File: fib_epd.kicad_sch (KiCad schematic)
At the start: 58 parts, among them J4 ED060SC4, J5 ED060SC7, J6 ED097OC4, J7 30PIN_05PITCH, U1 TPS651851RSLT, U4 ESP32-S3-WROOM-1U

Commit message: added port expander and level shifters, routed peripherals fixed most drc errors, assigned gpios etc.
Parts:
- R7: footprint Resistor_SMD:R_0402_1005Metric -> Resistor_SMD:R_0603_1608Metric
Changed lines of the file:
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@@
 			)
 		)
-		(property "Footprint" "Resistor_SMD:R_0402_1005Metric"
+		(property "Footprint" "Resistor_SMD:R_0603_1608Metric"
 			(at 29.21 33.02 0)
 			(effects

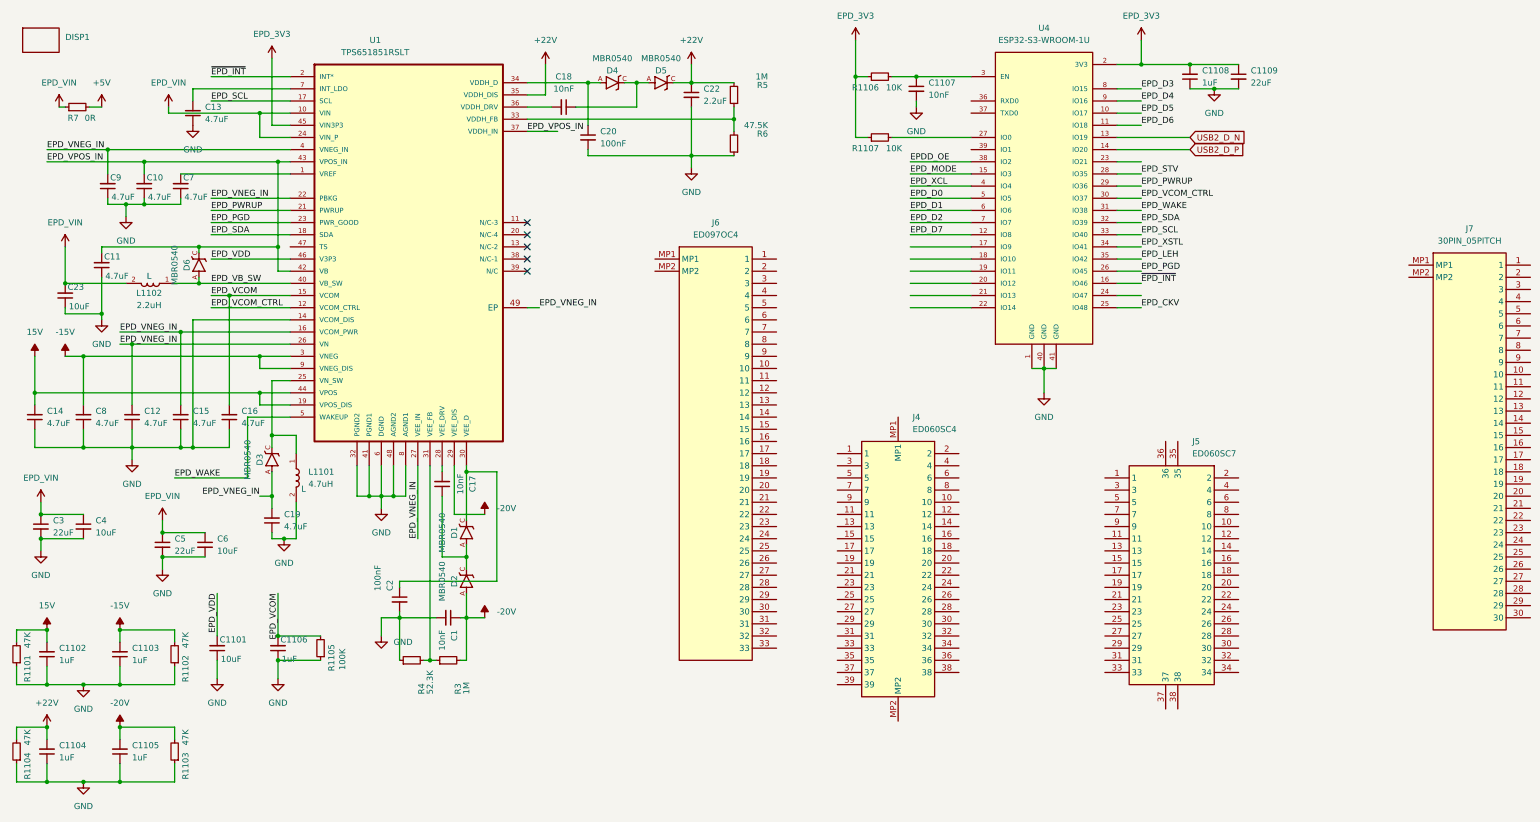
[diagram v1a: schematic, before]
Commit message: routed epd displays, added testpoints and all the little checks and fixe, (regrettably) removed the i80 connector, 99% there, need to double check some things add peripheral connectors, shared-ish storage and vias vias vias
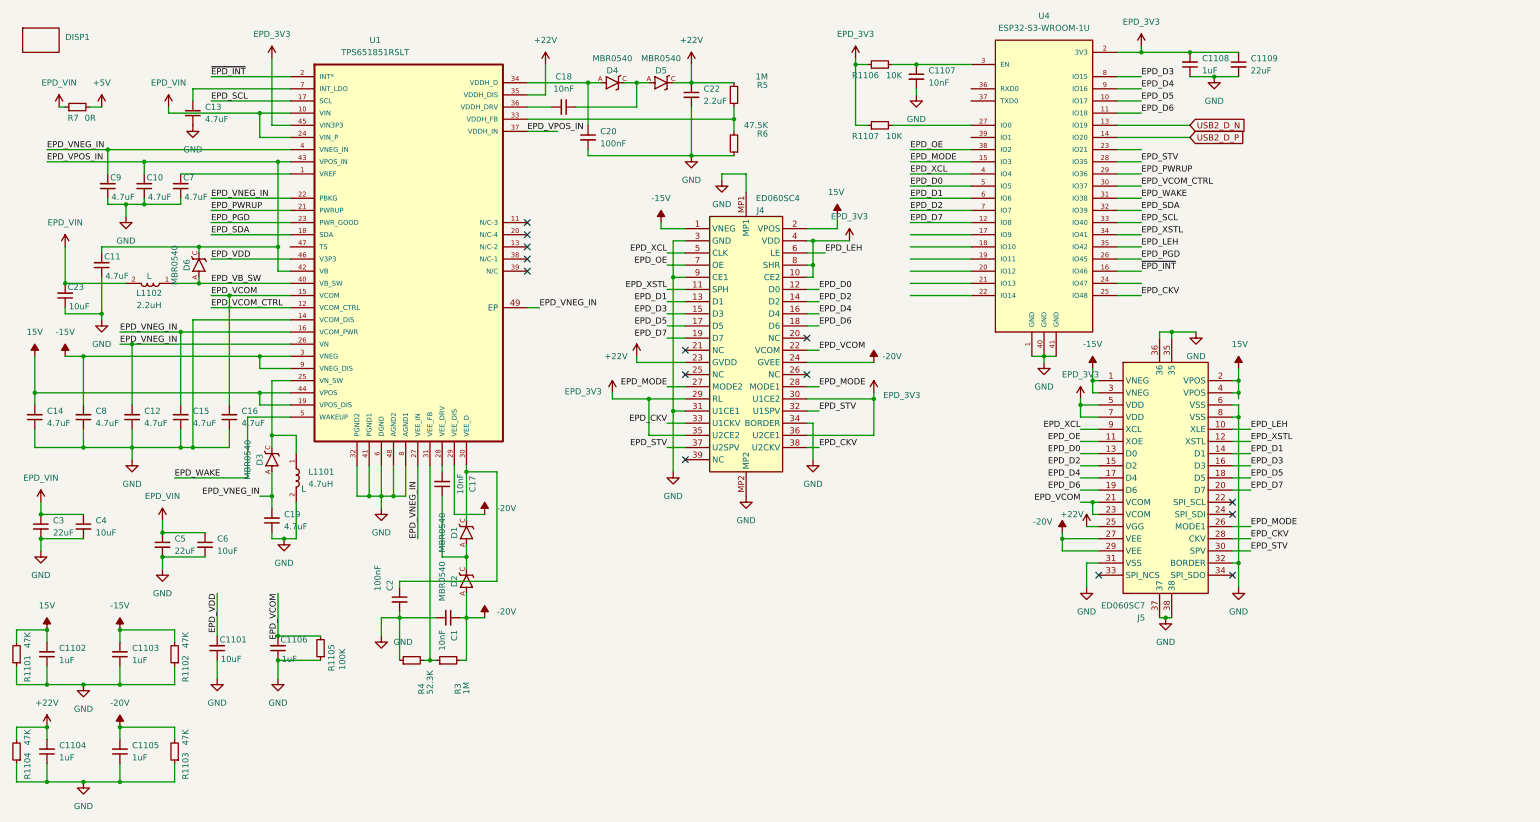
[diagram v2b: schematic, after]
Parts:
- removed J6: ED097OC4, Fibel2:ED097OC4, symbol Fibel2:ED097OC4
- removed J7: 30PIN_05PITCH, Fibel2:30PIN_05PITCH, symbol Fibel2:30PIN_05PITCH
- J4: Height (none) -> 3.1
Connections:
- net EPDD_OE is gone; now on net EPD_OE: U4.38 (IO2)
- net +22V: now also J4.23 (GVDD), J5.25 (VGG)
- net -15V: now also J4.1 (VNEG), J5.1 (VNEG), J5.3 (VNEG)
- net -20V: now also J4.24 (GVEE), J5.27 (VEE), J5.29 (VEE)
- net 15V: now also J4.2 (VPOS), J5.2 (VPOS), J5.4 (VPOS)
- net EPD_3V3: now also J4.10 (CE2), J4.29 (RL), J4.30 (U1CE2), J4.35 (U2CE2), J4.36 (U2CE1), J4.4 (VDD), J4.8 (SHR), J5.5 (VDD), J5.7 (VDD)
- net EPD_CKV: now also J4.33 (U1CKV), J4.38 (U2CKV), J5.28 (CKV)
- net EPD_D0: now also J4.12 (D0), J5.13 (D0)
- net EPD_D1: now also J4.13 (D1), J5.14 (D1)
- net EPD_D2: now also J4.14 (D2), J5.15 (D2)
- net EPD_D3: now also J4.15 (D3), J5.16 (D3)
- net EPD_D4: now also J4.16 (D4), J5.17 (D4)
- net EPD_D5: now also J4.17 (D5), J5.18 (D5)
- net EPD_D6: now also J4.18 (D6), J5.19 (D6)
- net EPD_D7: now also J4.19 (D7), J5.20 (D7)
- net EPD_LEH: now also J4.6 (LE), J5.10 (XLE)
- net EPD_MODE: now also J4.27 (MODE2), J4.28 (MODE1), J5.26 (MODE1)
- net EPD_STV: now also J4.32 (U1SPV), J4.37 (U2SPV), J5.30 (SPV)
- net EPD_VCOM: now also J4.22 (VCOM), J5.21 (VCOM), J5.23 (VCOM)
- net EPD_XCL: now also J4.5 (CLK), J5.9 (XCL)
- net EPD_XSTL: now also J4.11 (SPH), J5.12 (XSTL)
- net GND: now also J4.3 (GND), J4.31 (U1CE1), J4.34 (BORDER), J4.9 (CE1), J4.MP1, J4.MP2, J5.31 (VSS), J5.32 (BORDER), J5.35, J5.36, J5.37, J5.38, J5.6 (VSS), J5.8 (VSS)
- net EPD_OE: now reaches J5.11 (XOE)
- net EPD_OE: now also J4.7 (OE)
- no-connect marks 5 -> 14
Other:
- moved on the sheet: C1107, C1108, C1109, J4, R1106, R1107, U4

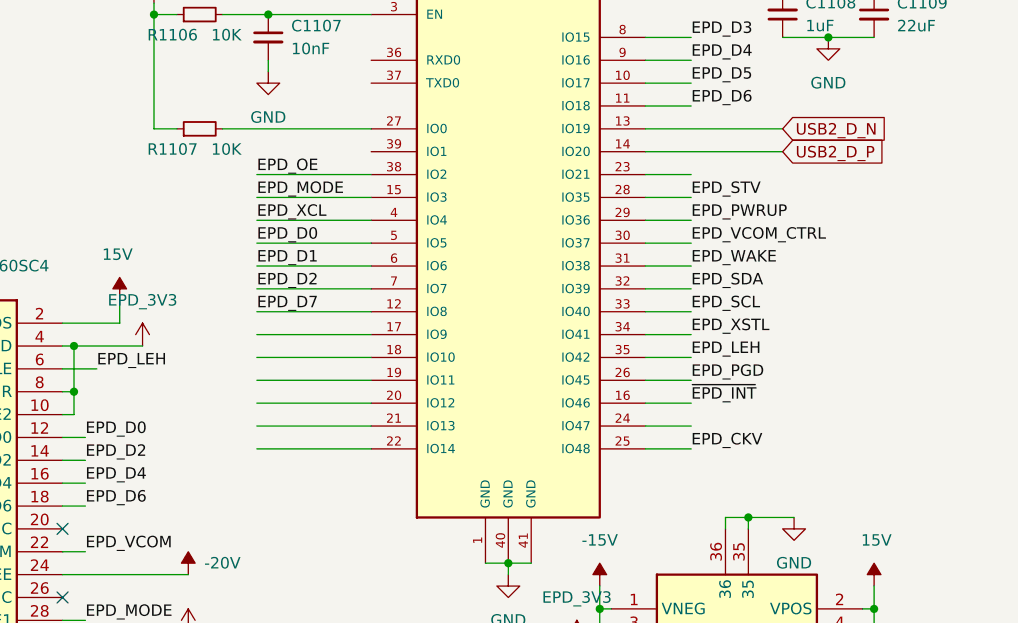
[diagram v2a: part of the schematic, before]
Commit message: finished routing, sanity check and prep fabrication files next
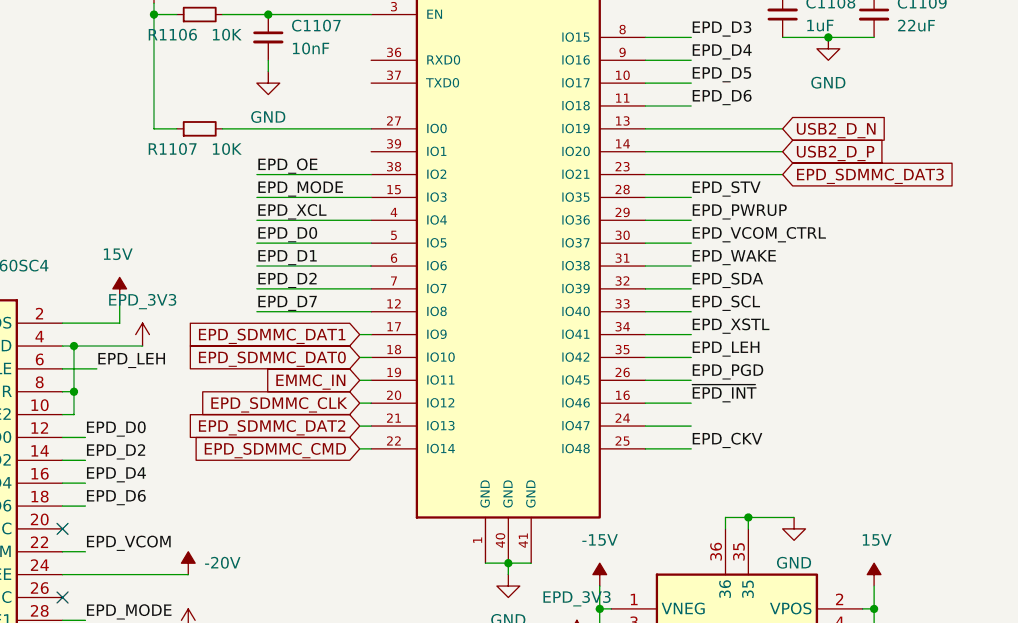
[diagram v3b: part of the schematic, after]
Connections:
- net EPD_SDMMC_DAT1: now reaches U4.17 (IO9)
- net EPD_SDMMC_DAT0: now reaches U4.18 (IO10)
- net EMMC_IN: now reaches U4.19 (IO11)
- net EPD_SDMMC_CLK: now reaches U4.20 (IO12)
- net EPD_SDMMC_DAT2: now reaches U4.21 (IO13)
- net EPD_SDMMC_CMD: now reaches U4.22 (IO14)
- net EPD_SDMMC_DAT3: now reaches U4.23 (IO21)
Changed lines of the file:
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@@
 	(wire
 		(pts
-			(xy 203.2 67.31) (xy 215.9 67.31)
+			(xy 214.63 67.31) (xy 215.9 67.31)
 		)
 		(stroke
@@
 	(wire
 		(pts
-			(xy 251.46 41.91) (xy 246.38 41.91)
+			(xy 261.62 41.91) (xy 246.38 41.91)
 		)
 		(stroke
@@
 	(wire
 		(pts
-			(xy 203.2 72.39) (xy 215.9 72.39)
+			(xy 214.63 72.39) (xy 215.9 72.39)
 		)
 		(stroke
@@
 	(wire
 		(pts
-			(xy 203.2 64.77) (xy 215.9 64.77)
+			(xy 214.63 64.77) (xy 215.9 64.77)
 		)
 		(stroke
@@
 	(wire
 		(pts
-			(xy 203.2 59.69) (xy 215.9 59.69)
+			(xy 214.63 59.69) (xy 215.9 59.69)
 		)
 		(stroke
@@
 	(wire
 		(pts
-			(xy 203.2 69.85) (xy 215.9 69.85)
+			(xy 214.63 69.85) (xy 215.9 69.85)
 		)
 		(stroke
@@
 	(wire
 		(pts
-			(xy 203.2 62.23) (xy 215.9 62.23)
+			(xy 214.63 62.23) (xy 215.9 62.23)
 		)
 		(stroke
@@
 		)
 	)
+	(global_label "EPD_SDMMC_DAT1"
+		(shape input)
+		(at 214.63 59.69 180)
+		(fields_autoplaced yes)
+		(effects
+			(font
+				(size 1.27 1.27)
+			)
+			(justify right)
+		)
+		(property "Intersheetrefs" "${INTERSHEET_REFS}"
+			(at 193.9858 59.69 0)
+			(effects
+				(font
+					(size 1.27 1.27)
+				)
+				(justify right)
+			)
+		)
+	)
 	(global_label "USB2_D_P"
 		(shape input)
@@
 		)
 	)
+	(global_label "EPD_SDMMC_CMD"
+		(shape input)
+		(at 214.63 72.39 180)
+		(fields_autoplaced yes)
+		(effects
+			(font
+				(size 1.27 1.27)
+			)
+			(justify right)
+		)
+		(property "Intersheetrefs" "${INTERSHEET_REFS}"
+			(at 194.5301 72.39 0)
+			(effects
+				(font
+					(size 1.27 1.27)
+				)
+				(justify right)
+			)
+		)
+	)
 	(global_label "USB2_D_N"
 		(shape input)
@@
 			)
 		)
+	)
+	(global_label "EPD_SDMMC_CLK"
+		(shape input)
+		(at 214.63 67.31 180)
+		(fields_autoplaced yes)
+		(effects
+			(font
+				(size 1.27 1.27)
+			)
+			(justify right)
+		)
+		(property "Intersheetrefs" "${INTERSHEET_REFS}"
+			(at 194.9534 67.31 0)
+			(effects
+				(font
+					(size 1.27 1.27)
+				)
+				(justify right)
+			)
+		)
+	)
+	(global_label "EPD_SDMMC_DAT2"
+		(shape input)
+		(at 214.63 69.85 180)
+		(fields_autoplaced yes)
+		(effects
+			(font
+				(size 1.27 1.27)
+			)
+			(justify right)
+		)
+		(property "Intersheetrefs" "${INTERSHEET_REFS}"
+			(at 193.9858 69.85 0)
+			(effects
+				(font
+					(size 1.27 1.27)
+				)
+				(justify right)
+			)
+		)
+	)
+	(global_label "EPD_SDMMC_DAT3"
+		(shape input)
+		(at 261.62 41.91 0)
+		(fields_autoplaced yes)
+		(effects
+			(font
+				(size 1.27 1.27)
+			)
+			(justify left)
+		)
+		(property "Intersheetrefs" "${INTERSHEET_REFS}"
+			(at 281.4174 41.91 0)
+			(effects
+				(font
+					(size 1.27 1.27)
+				)
+				(justify left)
+			)
+		)
+	)
+	(global_label "EPD_SDMMC_DAT0"
+		(shape input)
+		(at 214.63 62.23 180)
+		(fields_autoplaced yes)
+		(effects
+			(font
+				(size 1.27 1.27)
+			)
+			(justify right)
+		)
+		(property "Intersheetrefs" "${INTERSHEET_REFS}"
+			(at 193.9858 62.23 0)
+			(effects
+				(font
+					(size 1.27 1.27)
+				)
+				(justify right)
+			)
+		)
+	)
+	(global_label "EMMC_IN"
+		(shape input)
+		(at 214.63 64.77 180)
+		(fields_autoplaced yes)
+		(effects
+			(font
+				(size 1.27 1.27)
+			)
+			(justify right)
+		)
+		(property "Intersheetrefs" "${INTERSHEET_REFS}"
+			(at 203.4201 64.77 0)
+			(effects
+				(font
+					(size 1.27 1.27)
+				)
+				(justify right)
+			)
+		)

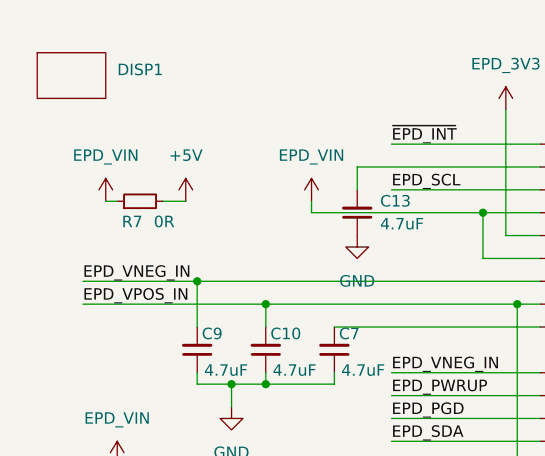
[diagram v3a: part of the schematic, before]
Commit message: added second i2c, modified 40 pin headers
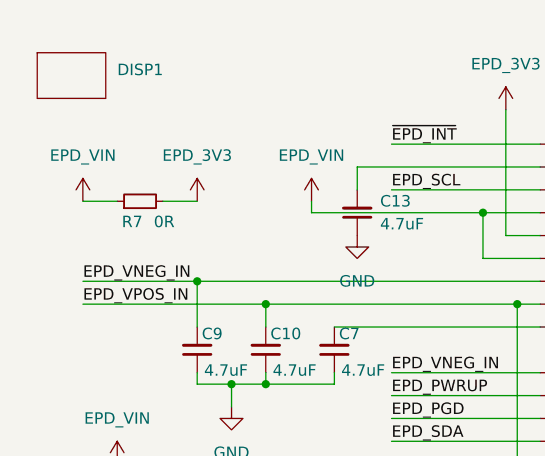
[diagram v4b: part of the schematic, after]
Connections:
- net +5V is gone; now on net EPD_3V3: R7.2
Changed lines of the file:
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@@
 	(wire
 		(pts
-			(xy 31.75 33.02) (xy 34.29 33.02)
+			(xy 31.75 33.02) (xy 35.56 33.02)
 		)
 		(stroke
@@
 	(wire
 		(pts
-			(xy 25.4 33.02) (xy 26.67 33.02)
+			(xy 22.86 33.02) (xy 26.67 33.02)
 		)
 		(stroke
@@
 		)
 		(instances
-			(project ""
+			(project "Fibel2"
 				(path "/862c21e2-7ec9-4f80-a33c-aad02ea9423e/5a179277-42b3-47ed-bc0e-bf53dbccdf92"
 					(reference "U4")
@@
 		)
 		(instances
-			(project ""
+			(project "Fibel2"
 				(path "/862c21e2-7ec9-4f80-a33c-aad02ea9423e/5a179277-42b3-47ed-bc0e-bf53dbccdf92"
 					(reference "J4")
@@
 	(symbol
 		(lib_id "power:+5V")
-		(at 34.29 33.02 0)
+		(at 35.56 33.02 0)
 		(unit 1)
 		(exclude_from_sim no)
@@
 		(fields_autoplaced yes)
 		(property "Reference" "#PWR027"
-			(at 34.29 36.83 0)
+			(at 35.56 36.83 0)
 			(effects
 				(font
@@
 			)
 		)
-		(property "Value" "+5V"
-			(at 34.29 27.94 0)
+		(property "Value" "EPD_3V3"
+			(at 35.56 27.94 0)
 			(effects
 				(font
@@
 		)
 		(property "Footprint" ""
-			(at 34.29 33.02 0)
+			(at 35.56 33.02 0)
 			(effects
 				(font
@@
 		)
 		(property "Datasheet" ""
-			(at 34.29 33.02 0)
+			(at 35.56 33.02 0)
 			(effects
 				(font
@@
 		)
 		(property "Description" "Power symbol creates a global label with name \"+5V\""
-			(at 34.29 33.02 0)
+			(at 35.56 33.02 0)
 			(effects
 				(font
@@
 		)
 		(instances
-			(project ""
+			(project "Fibel2"
 				(path "/862c21e2-7ec9-4f80-a33c-aad02ea9423e/5a179277-42b3-47ed-bc0e-bf53dbccdf92"
 					(reference "DISP1")
@@
 	(symbol
 		(lib_id "power:+5V")
-		(at 25.4 33.02 0)
+		(at 22.86 33.02 0)
 		(unit 1)
 		(exclude_from_sim no)
@@
 		(fields_autoplaced yes)
 		(property "Reference" "#PWR026"
-			(at 25.4 36.83 0)
+			(at 22.86 36.83 0)
 			(effects
 				(font
@@
 		)
 		(property "Value" "EPD_VIN"
-			(at 25.4 27.94 0)
+			(at 22.86 27.94 0)
 			(effects
 				(font
@@
 		)
 		(property "Footprint" ""
-			(at 25.4 33.02 0)
+			(at 22.86 33.02 0)
 			(effects
 				(font
@@
 		)
 		(property "Datasheet" ""
-			(at 25.4 33.02 0)
+			(at 22.86 33.02 0)
 			(effects
 				(font
@@
 		)
 		(property "Description" "Power symbol creates a global label with name \"+5V\""
-			(at 25.4 33.02 0)
+			(at 22.86 33.02 0)
 			(effects
 				(font
